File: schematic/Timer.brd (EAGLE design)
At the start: 100 x 80 mm, 30 parts, among them IC1 MEGA8-AI, J1 AVR_SPI_PRG_6NS, Q1 BC807-40SMD, Q2 BC807-40SMD, Q3 BC807-40SMD, Q4 BC807-40SMD

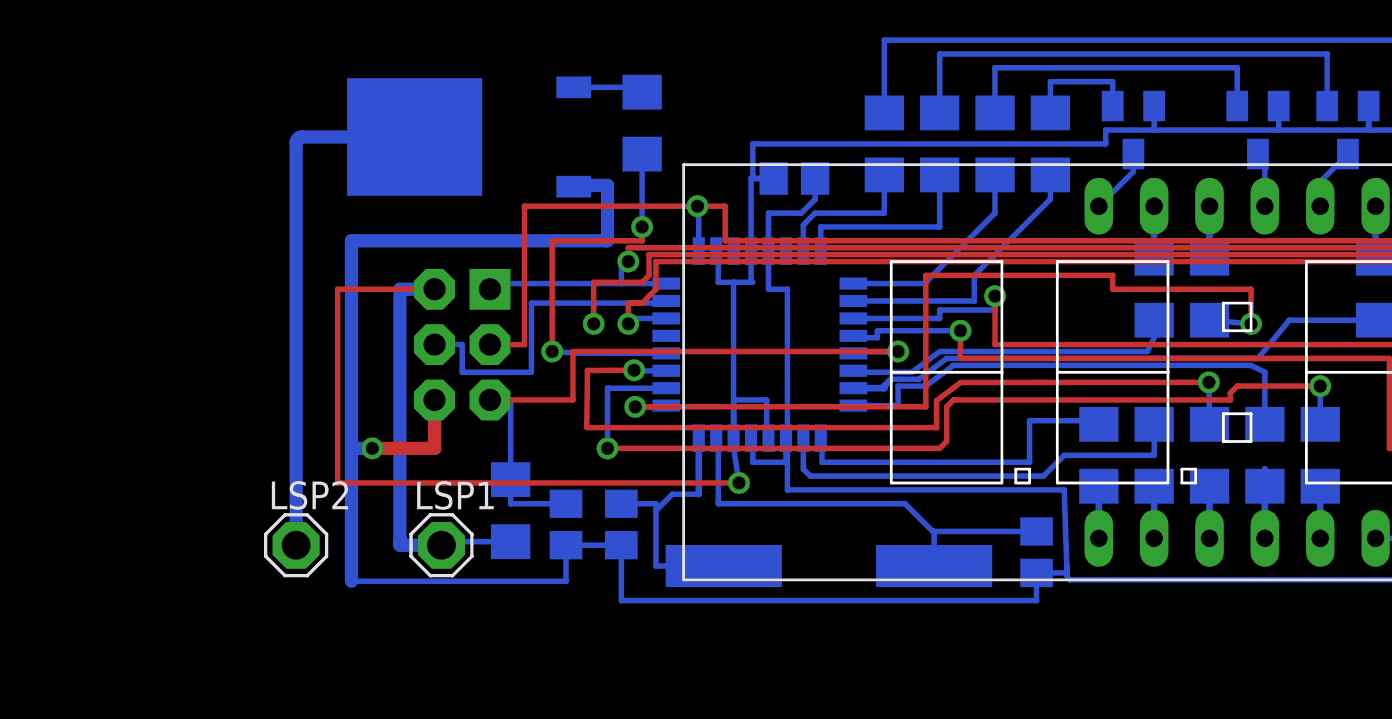
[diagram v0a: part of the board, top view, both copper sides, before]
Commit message: изменения в схеме
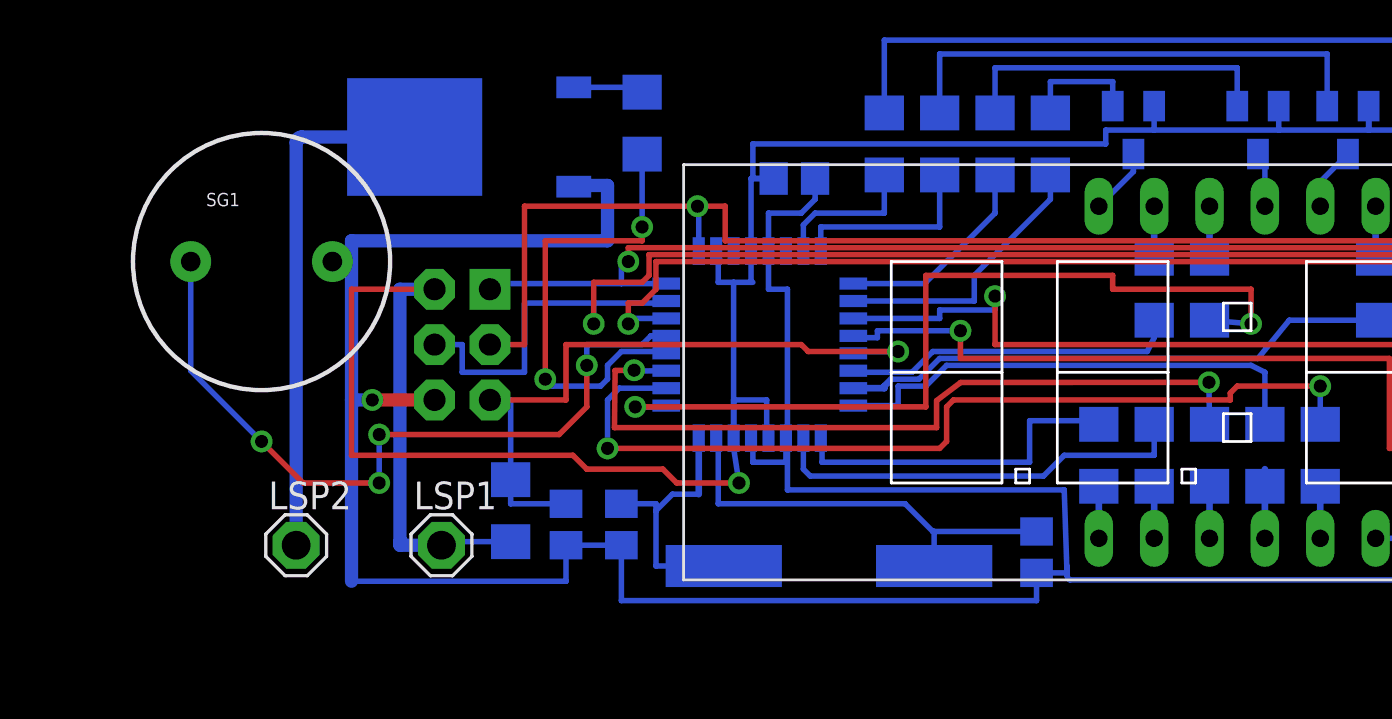
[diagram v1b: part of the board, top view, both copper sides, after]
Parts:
- added SG1: BUZZERPTH-KIT, SparkFun-Electromechanical:BUZZER-12MM-KIT
- R10: value 1k5 -> 10k
- R2, R3, R4, R5, R6, R7, R8, R9: value 1k5 -> 330
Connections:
- new net BUZZ: IC1.13, SG1.-
- net GND: now also SG1.+
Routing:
- net BUZZ: track 0.00 -> 34.7 mm, vias 0 -> 4
- net RELAY: track 18.4 -> 21.5 mm
- net DP: track 38.2 -> 35.7 mm
- net VCC: track 141.8 -> 139.8 mm
- net GND: track 158.5 -> 157.8 mm
